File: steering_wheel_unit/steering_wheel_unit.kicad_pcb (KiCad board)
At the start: 2 copper layers, 112 x 94.5 mm, 130 parts, among them IC2 LM76202QPWPRQ1, J1 MAIN_CONNECTOR, J10 MODE2_SOCKET, J11 FUEL_CELL_SOCKET, J12 USB_C_Vertical, J13 Additional goldpins, J14 LCD_SOCKET, J15 JTAG_SOCKET, J16 Additional goldpins from MCU, J3 HALF_GAS_SOCKET, J4 MODE1_SOCKET, J5 FULL_GAS_SOCKET, J6 SPEED_RESET_SOCKET, J7 HORN_SOCKET, J8 SC_CLOSE_SOCKET, J9 SUPPLY_SOCKET, SW1 TL3305BF100QG, SW2 TL3305BF100QG, SW3 TL3305BF100QG, U1 STM32G491CCTx, U2 USBLC6-2P6, U3 SN65HVD232, U4 TPS62933, X1 32k768, X2 24M

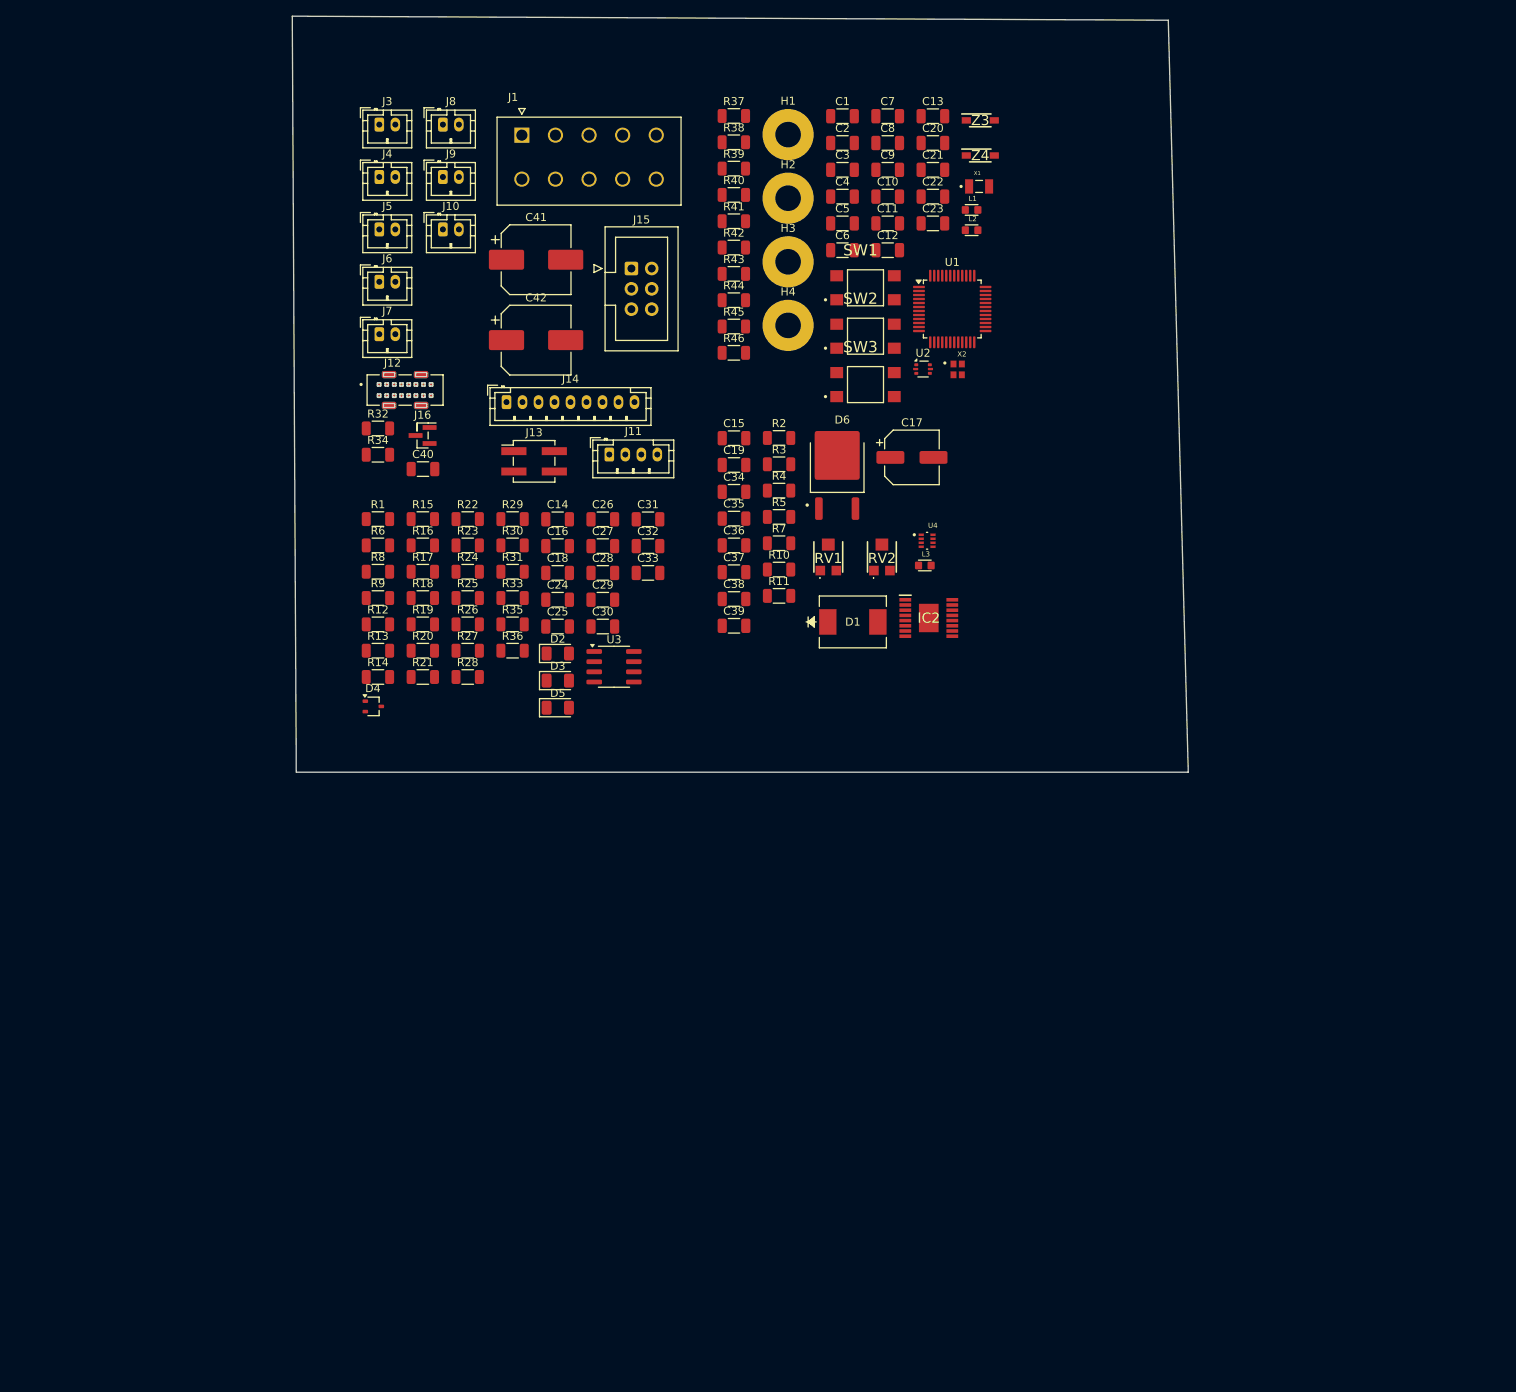
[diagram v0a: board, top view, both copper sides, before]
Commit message: add edge cuts and rough components layout
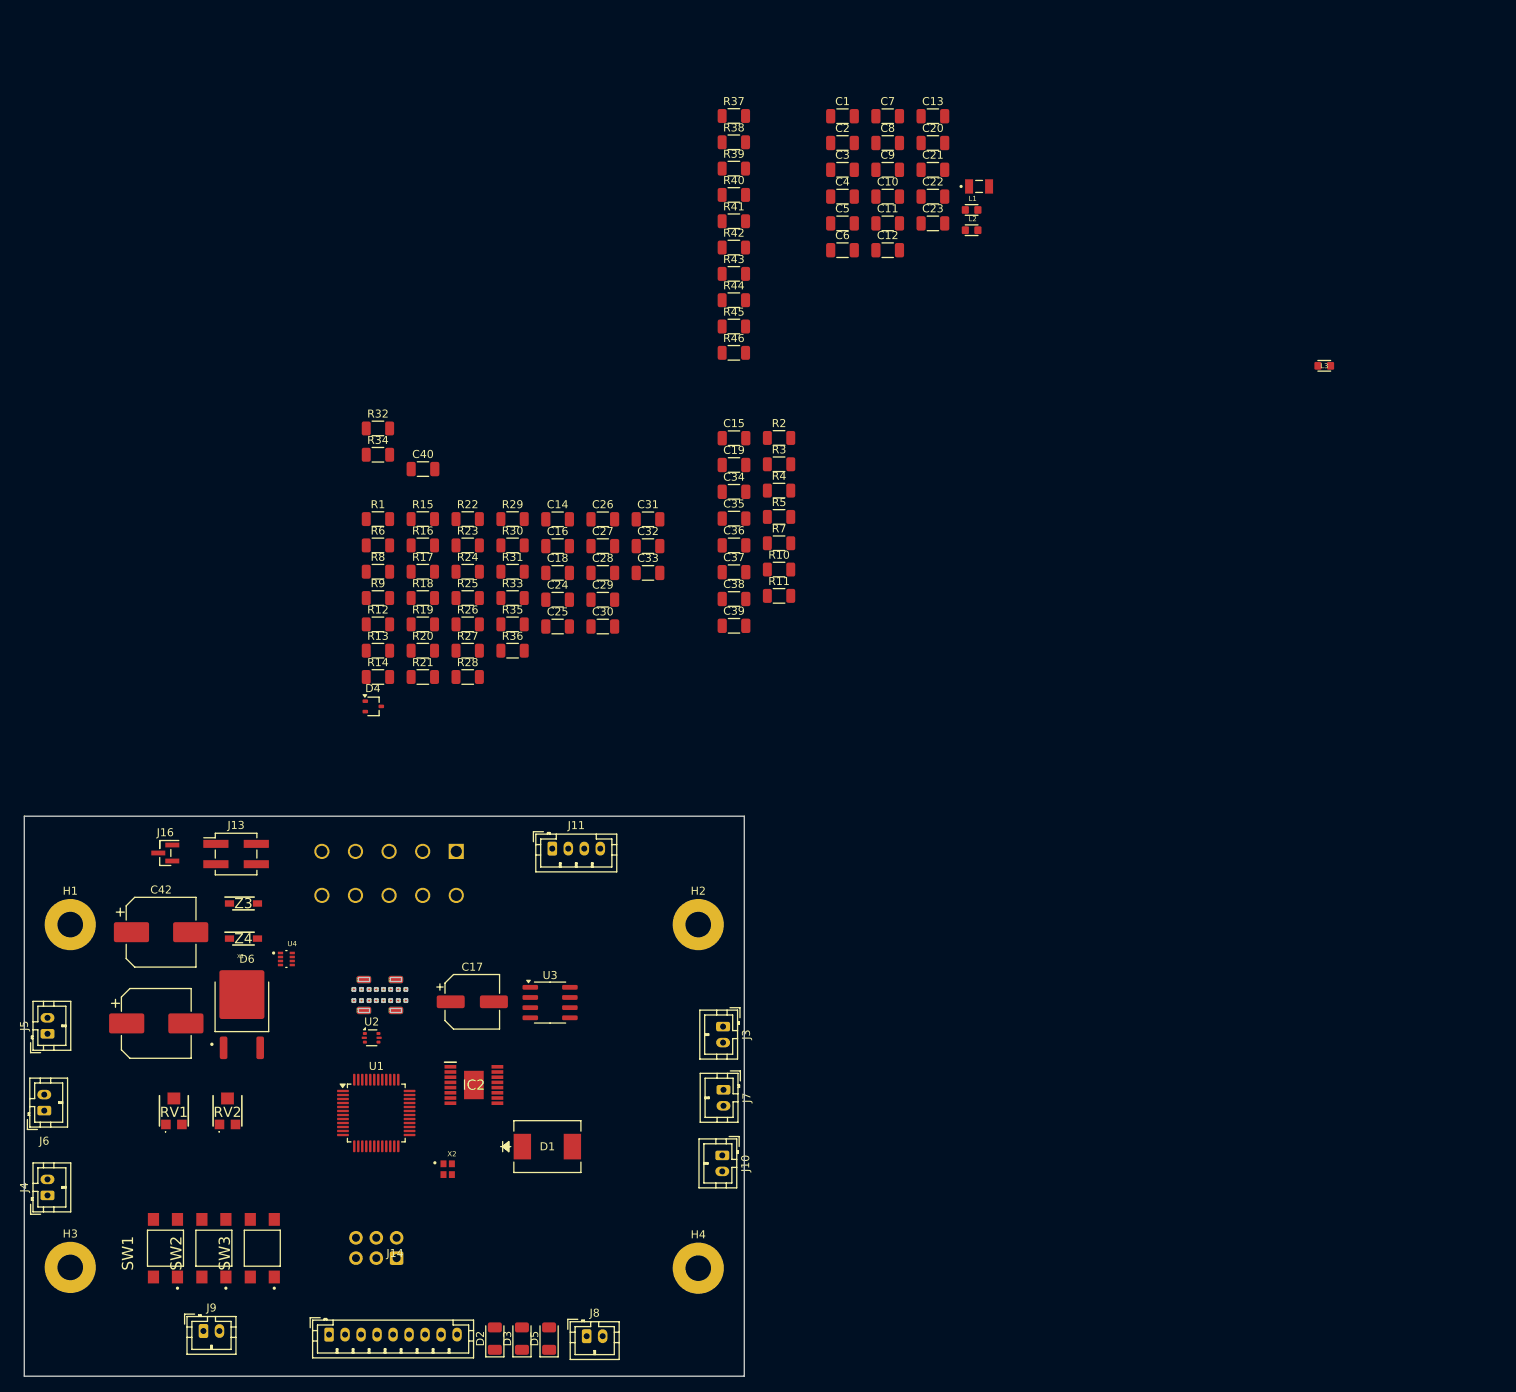
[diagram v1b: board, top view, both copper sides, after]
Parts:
- J1, J12, J15: moved to B.Cu
- moved H3 154.4 mm to (55.2, 183.9)
- moved J8 152.5 mm to (119.8, 192.5)
- moved SW1 148.6 mm to (67.2, 181.5), turned to 90 degrees
- moved J9 147.3 mm to (71.9, 191.8)
- moved SW2 140.1 mm to (73.2, 181.5), turned to 90 degrees
- moved Z4 134.4 mm to (76.9, 142.8)
- moved Z3 134.4 mm to (76.9, 138.4)
- moved J4 133.9 mm to (52.4, 174.9), turned to 90 degrees
- moved H1 133.4 mm to (55.2, 141.1)
- moved SW3 131.7 mm to (79.2, 181.5), turned to 90 degrees
- moved J15 127.1 mm to (96.0, 182.7), turned to 90 degrees
- moved U1 123.6 mm to (93.5, 164.6)
- moved J10 120.9 mm to (136.8, 169.9), turned to -90 degrees
- moved J3 120.7 mm to (136.8, 153.8), turned to -90 degrees
- moved J14 118.7 mm to (87.6, 192.3)
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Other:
- board size 112 x 94.5 mm -> 90 x 70 mm

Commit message: organize the preliminary layout
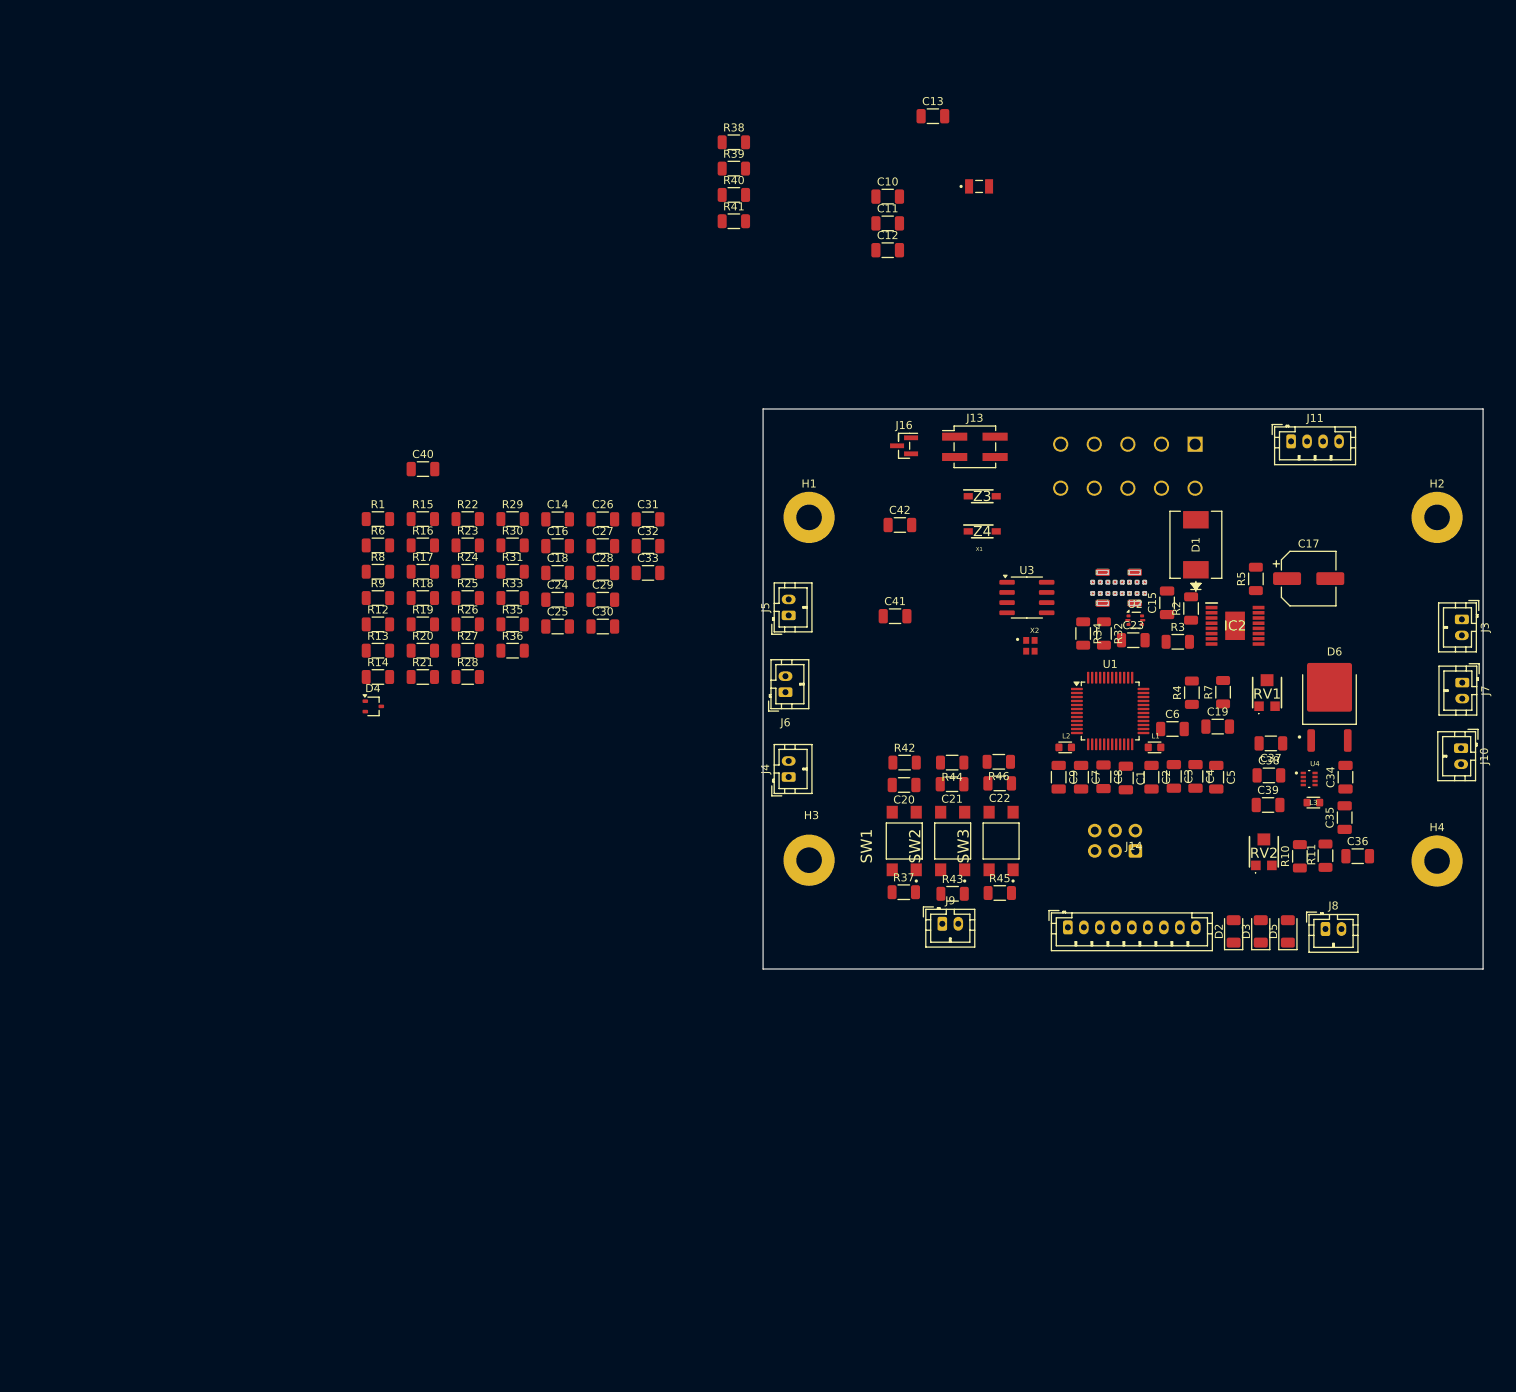
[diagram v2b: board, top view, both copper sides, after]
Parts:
- C41, C42: footprint Capacitor_SMD:CP_Elec_8x10.5 -> Capacitor_SMD:C_1206_3216Metric
- moved RV1 146.3 mm to (204.8, 112.0)
- moved D6 141.3 mm to (212.7, 113.9)
- moved RV2 133.5 mm to (204.4, 131.9)
- moved U4 129.8 mm to (210.1, 122.8)
- moved C17 117.2 mm to (210.1, 97.8)
- moved IC2 111.1 mm to (200.8, 103.7)
- moved D1 110.6 mm to (195.9, 93.6), turned to 90 degrees
- moved U2 108.8 mm to (188.4, 103.0)
- moved J4 106.4 mm to (145.1, 122.6)
- moved J6 106.4 mm to (144.7, 112.0)
- moved J5 106.4 mm to (145.1, 102.4)
- moved D3 105.4 mm to (204.1, 141.9)
- moved J12 105.4 mm to (186.3, 99.0)
- moved J8 105.4 mm to (212.2, 141.6)
- moved SW2 105.4 mm to (165.6, 130.6)
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
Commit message: edit layout
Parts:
- moved R14 128.2 mm to (221.8, 104.4), turned to 180 degrees
- moved R16 123.8 mm to (221.9, 111.3)
- moved R17 123.7 mm to (221.8, 113.8), turned to 180 degrees
- moved R15 123.0 mm to (221.7, 101.9)
- moved R8 120.8 mm to (213.9, 85.4)
- moved R1 120.3 mm to (213.9, 88.1)
- moved R20 119.6 mm to (215.2, 136.4), turned to -90 degrees
- moved R24 119.1 mm to (221.7, 120.3)
- moved R28 117.5 mm to (221.7, 122.8), turned to 180 degrees
- moved R9 116.2 mm to (209.0, 85.4)
- moved R21 115.6 mm to (211.5, 137.7), turned to 180 degrees
- moved R6 115.4 mm to (209.0, 88.1)
- moved R30 103.4 mm to (213.9, 90.7)
- moved R36 103.3 mm to (207.4, 142.7), turned to -90 degrees
- moved C29 102.4 mm to (217.7, 136.4), turned to -90 degrees
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
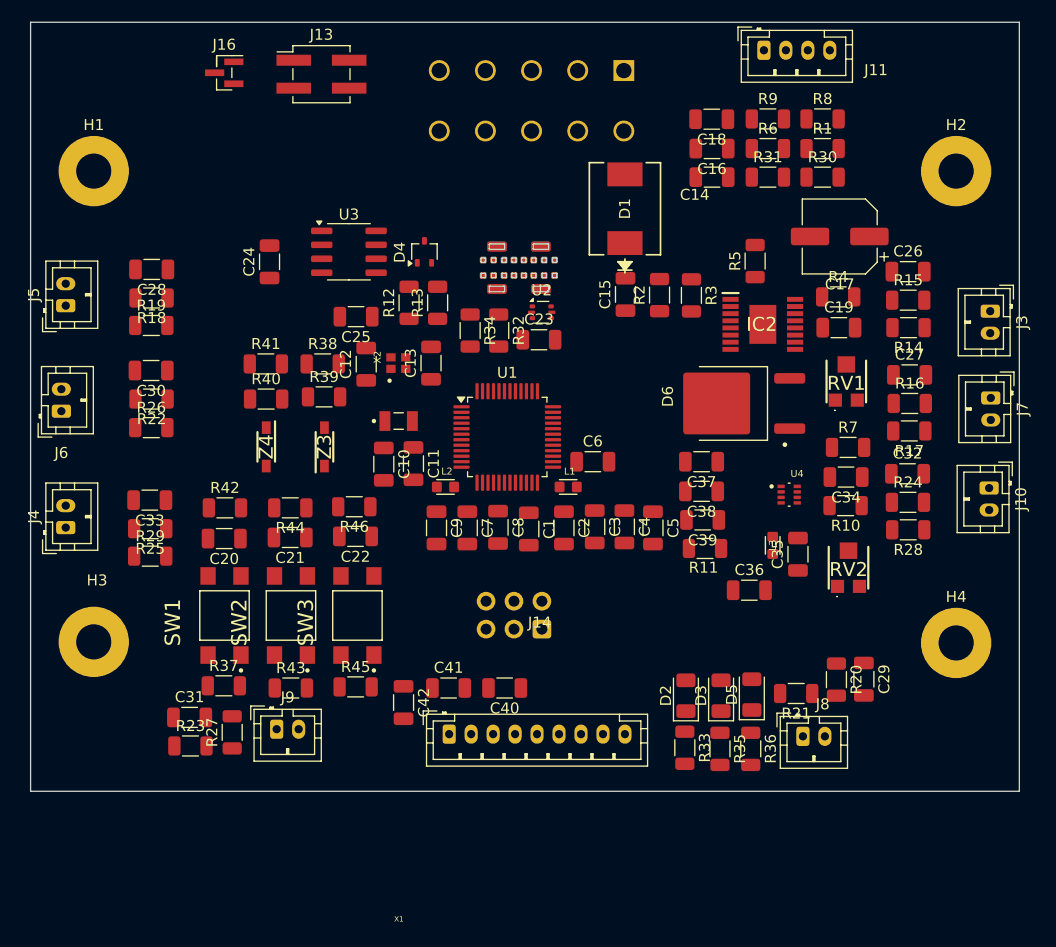
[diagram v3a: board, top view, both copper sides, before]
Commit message: Draw part of paths
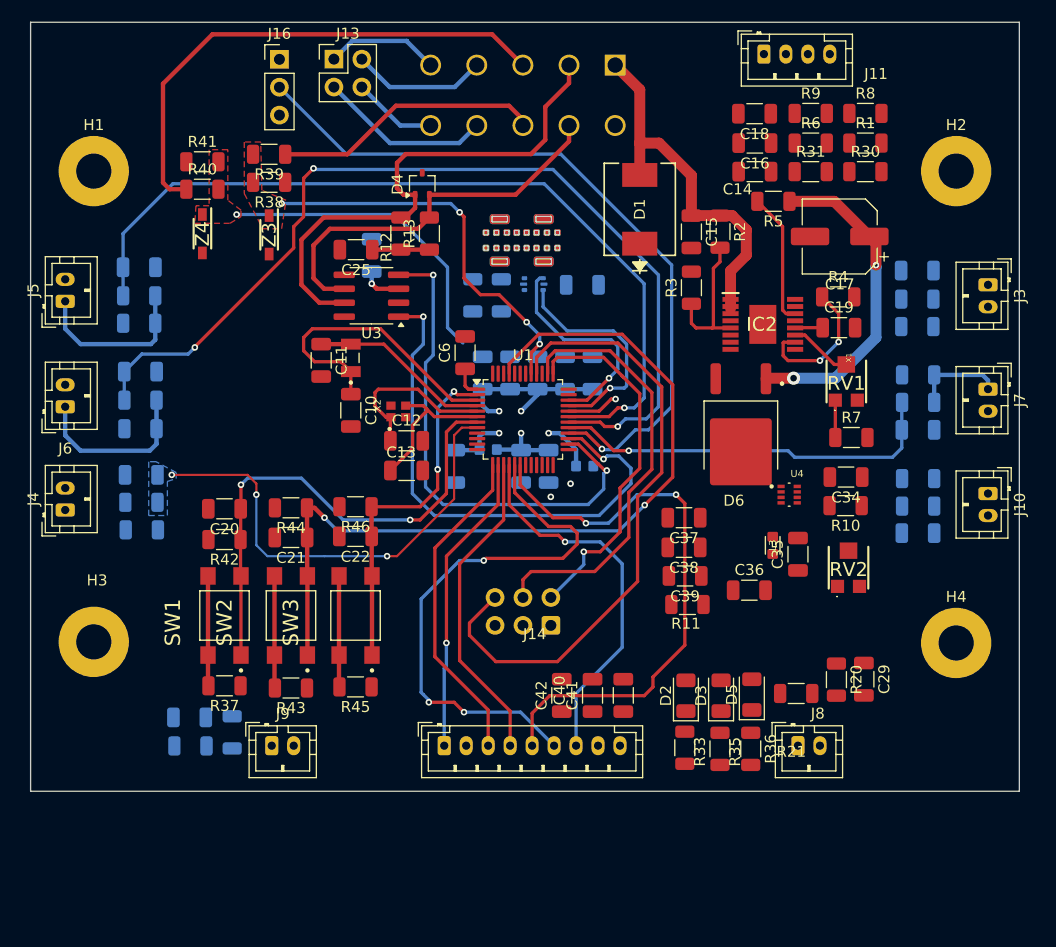
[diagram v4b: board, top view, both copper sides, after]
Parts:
- C1, C2, C23, C24, C26, C27, C28, C3, C30, C31, C32, C33, C4, C5, C7, C8, C9, L1, L2, R14, R15, R16, R17, R18, R19, R22, R23, R24, R25, R26, R27, R28, R29, R32, R34, U2: moved to B.Cu
- J13: footprint Connector_PinHeader_2.54mm:PinHeader_2x02_P2.54mm_Vertical_SMD -> Connector_PinHeader_2.54mm:PinHeader_2x02_P2.54mm_Vertical
- J16: footprint Connector_PinHeader_1.00mm:PinHeader_1x03_P1.00mm_Vertical_SMD_Pin1Right -> Connector_PinHeader_2.54mm:PinHeader_1x03_P2.54mm_Vertical
- moved R39 22.6 mm to (163.6, 88.6), turned to 180 degrees
- moved Z4 20.3 mm to (157.5, 95.8)
- moved R40 20.0 mm to (157.5, 91.8)
- moved Z3 19.9 mm to (163.6, 96.0), turned to -90 degrees
- moved R41 19.3 mm to (157.5, 89.3)
- moved R38 17.2 mm to (163.6, 91.2), turned to 180 degrees
- moved C6 15.3 mm to (181.4, 106.7), turned to 90 degrees
- moved C5 15.1 mm to (193.0, 108.5), turned to 90 degrees
- moved C4 15.0 mm to (190.5, 108.5), turned to 90 degrees
- moved C3 14.9 mm to (188.0, 108.5), turned to 90 degrees
- moved C2 14.9 mm to (185.5, 108.5), turned to 90 degrees
- moved C1 14.8 mm to (183.0, 108.5), turned to 90 degrees
- moved C42 14.4 mm to (190.2, 137.9), turned to 90 degrees
- moved C41 13.1 mm to (193.0, 137.9), turned to 90 degrees
- moved C11 12.6 mm to (168.3, 107.4)
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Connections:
- J1 pad 2: GND -> /CANH
- J1 pad 3: /CANH -> /GPIO1
- J1 pad 4: /CANL -> Net-(J1-Pin_4)
- J1 pad 5: /GPIO2 -> Net-(J1-Pin_5)
- J1 pad 6: /GPIO1 -> GND
- J1 pad 7: Net-(J1-Pin_7) -> /CANL
- J1 pad 8: Net-(J1-Pin_8) -> /GPIO2
- J13 pad 1: Net-(J1-Pin_9) -> Net-(J1-Pin_5)
- J13 pad 2: Net-(J1-Pin_10) -> Net-(J1-Pin_4)
- J13 pad 3: Net-(J1-Pin_7) -> Net-(J1-Pin_9)
- J13 pad 4: Net-(J1-Pin_8) -> Net-(J1-Pin_10)
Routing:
- net /IO/SPEED_RESET_BUTTON_MCU: track 0.00 -> 87.2 mm, vias 0 -> 3
- net /MCU/BOOT0: track 0.00 -> 76.8 mm, vias 0 -> 2
- net /IO/FULL_GAS_BUTTON_MCU: track 0.00 -> 76.7 mm, vias 0 -> 1
- net /MCU/GPIO_PB14: track 0.00 -> 66.9 mm, vias 0 -> 1
- net /SWO: track 0.00 -> 57.4 mm
- net /LCD_DC: track 0.00 -> 52.5 mm, vias 0 -> 2
- net /LCD_RST: track 0.00 -> 49.7 mm, vias 0 -> 3
- net /IO/CAN_RX: track 0.00 -> 49.1 mm, vias 0 -> 2
- net /CANH: track 0.00 -> 47.7 mm
- net /GPIO1: track 0.00 -> 47.2 mm
- net /IO/CAN_TX: track 0.00 -> 46.5 mm, vias 0 -> 2
- net /MCU/RESET: track 0.00 -> 45.9 mm, vias 0 -> 2
- net /IO/MODE1_BUTTON_MCU: track 0.00 -> 42.4 mm, vias 0 -> 3
- net /SWCLK: track 0.00 -> 39.7 mm
- net /CANL: track 0.00 -> 36.0 mm
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- added copper zone on B.Cu, net /IO/MODE1_BUTTON_MCU
- added copper zone on F.Cu, net /MCU/PA4
- added copper zone on F.Cu, net /MCU/PB4
